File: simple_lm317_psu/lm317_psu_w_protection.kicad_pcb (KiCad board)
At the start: 2 copper layers, 50 x 24.7 mm, 12 parts, among them J1 Bornera, U1 LM317

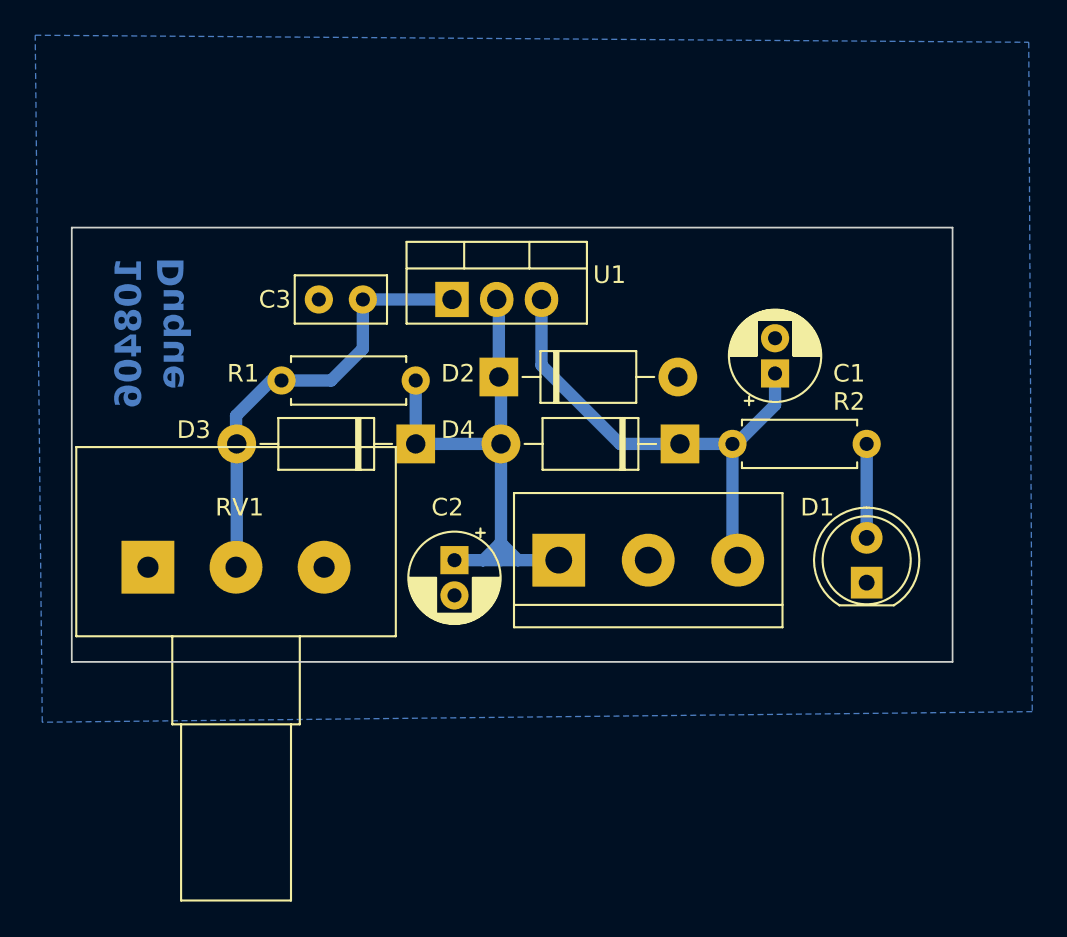
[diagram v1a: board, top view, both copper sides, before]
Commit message: [ADD] LM317 CV PSU (with minimal protecctions)
WIP - Add CC protections
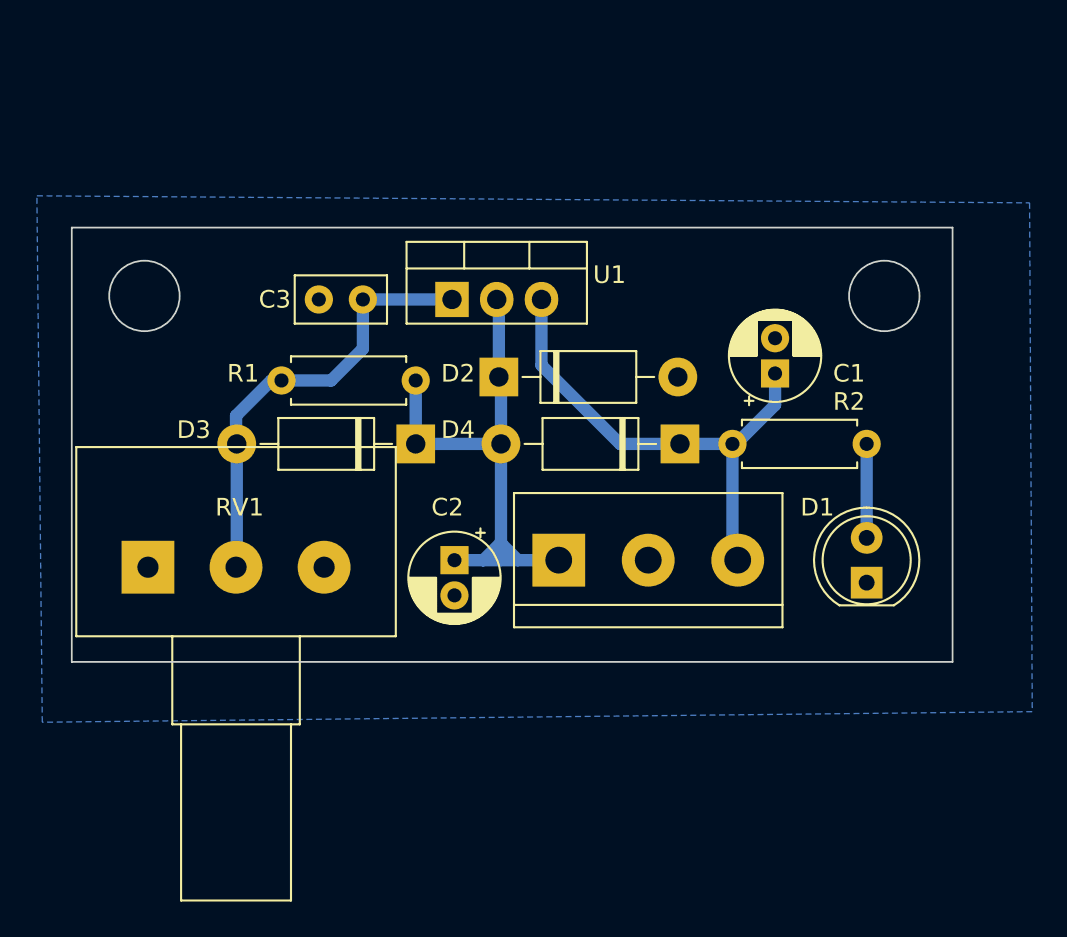
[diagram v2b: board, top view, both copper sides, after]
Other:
- outline, holes or cut-outs redrawn
- board text removed: "108406 Duque"
